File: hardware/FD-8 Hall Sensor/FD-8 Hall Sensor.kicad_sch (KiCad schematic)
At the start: 18 parts, among them J1 Panel connections, J2 ICSP Programming, J3 Hall sensor input, J4 Extra GPIO, U1 LM2940T-5.0_NOPB, U2 ATtiny13A-P, U3 MCP42100

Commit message: update PCB placement
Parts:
- C1, C10, C2, C3, C4, C5, C7, C8, C9: footprint Capacitor_THT:C_Disc_D4.7mm_W2.5mm_P5.00mm -> Capacitor_THT:C_Disc_D4.3mm_W1.9mm_P5.00mm
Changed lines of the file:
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@@
 			)
 		)
-		(property "Footprint" "Capacitor_THT:C_Disc_D4.7mm_W2.5mm_P5.00mm"
+		(property "Footprint" "Capacitor_THT:C_Disc_D4.3mm_W1.9mm_P5.00mm"
 			(at 115.57 48.26 0)
 			(effects
@@
 			)
 		)
-		(property "Footprint" "Capacitor_THT:C_Disc_D4.7mm_W2.5mm_P5.00mm"
+		(property "Footprint" "Capacitor_THT:C_Disc_D4.3mm_W1.9mm_P5.00mm"
 			(at 119.38 48.26 0)
 			(effects
@@
 			)
 		)
-		(property "Footprint" "Capacitor_THT:C_Disc_D4.7mm_W2.5mm_P5.00mm"
+		(property "Footprint" "Capacitor_THT:C_Disc_D4.3mm_W1.9mm_P5.00mm"
 			(at 190.5 48.26 0)
 			(effects
@@
 			)
 		)
-		(property "Footprint" "Capacitor_THT:C_Disc_D4.7mm_W2.5mm_P5.00mm"
+		(property "Footprint" "Capacitor_THT:C_Disc_D4.3mm_W1.9mm_P5.00mm"
 			(at 182.88 48.26 0)
 			(effects
@@
 			)
 		)
-		(property "Footprint" "Capacitor_THT:C_Disc_D4.7mm_W2.5mm_P5.00mm"
+		(property "Footprint" "Capacitor_THT:C_Disc_D4.3mm_W1.9mm_P5.00mm"
 			(at 130.81 48.26 0)
 			(effects
@@
 			)
 		)
-		(property "Footprint" "Capacitor_THT:C_Disc_D4.7mm_W2.5mm_P5.00mm"
+		(property "Footprint" "Capacitor_THT:C_Disc_D4.3mm_W1.9mm_P5.00mm"
 			(at 198.12 48.26 0)
 			(effects
@@
 			)
 		)
-		(property "Footprint" "Capacitor_THT:C_Disc_D4.7mm_W2.5mm_P5.00mm"
+		(property "Footprint" "Capacitor_THT:C_Disc_D4.3mm_W1.9mm_P5.00mm"
 			(at 127 48.26 0)
 			(effects
@@
 			)
 		)
-		(property "Footprint" "Capacitor_THT:C_Disc_D4.7mm_W2.5mm_P5.00mm"
+		(property "Footprint" "Capacitor_THT:C_Disc_D4.3mm_W1.9mm_P5.00mm"
 			(at 123.19 48.26 0)
 			(effects
@@
 			)
 		)
-		(property "Footprint" "Capacitor_THT:C_Disc_D4.7mm_W2.5mm_P5.00mm"
+		(property "Footprint" "Capacitor_THT:C_Disc_D4.3mm_W1.9mm_P5.00mm"
 			(at 127 99.06 0)
 			(effects

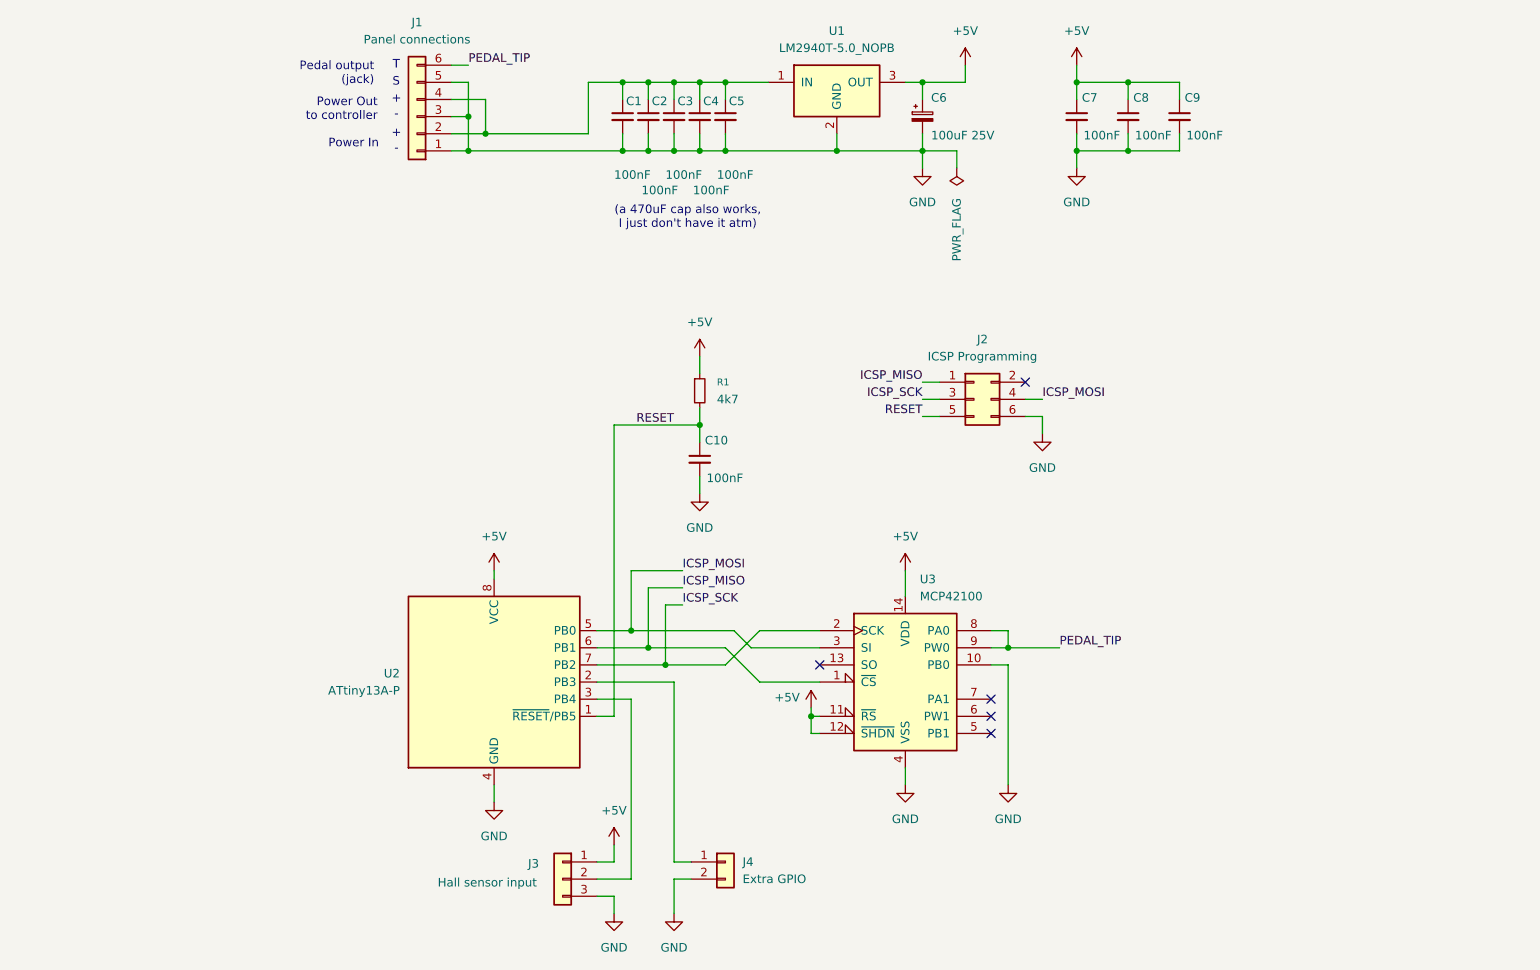
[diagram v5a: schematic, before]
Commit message: use MCP42010 (both pots) instead of MCP42100
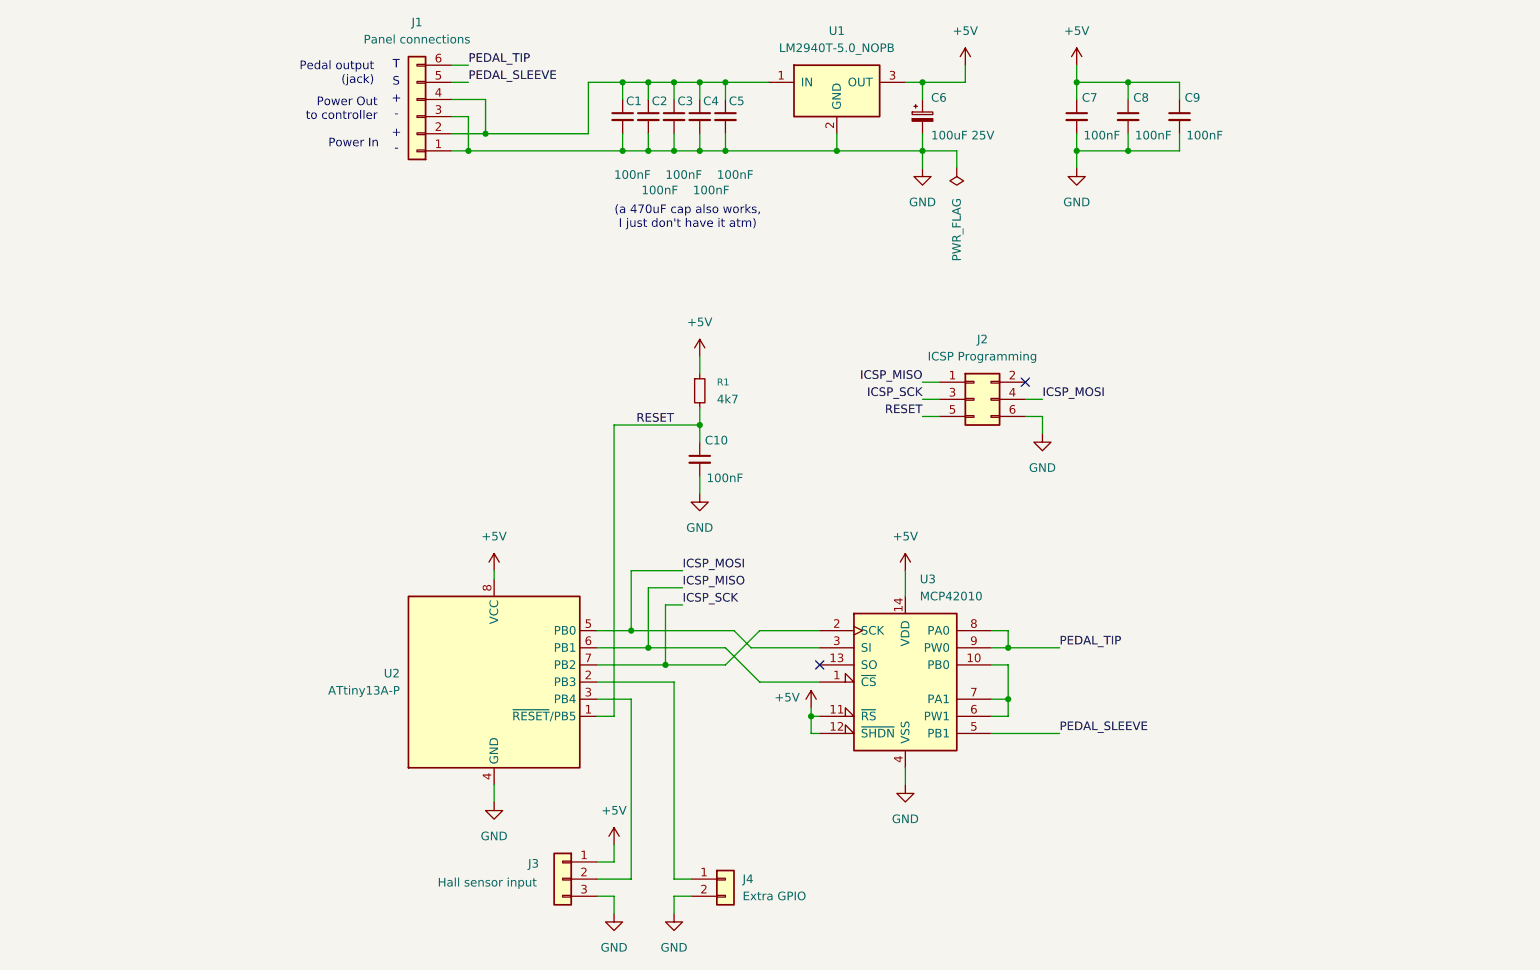
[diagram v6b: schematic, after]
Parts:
- removed U3: MCP42100, Package_DIP:DIP-14_W7.62mm, symbol Potentiometer_Digital:MCP42100
- added U3: MCP42010, Package_DIP:DIP-14_W7.62mm, symbol Potentiometer_Digital:MCP42010
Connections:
- net +5V: now also U3.11 (~{RS}), U3.12 (~{SHDN}), U3.14 (VDD)
- net GND: now also U3.4 (VSS); no longer J1.5 (Pin_5)
- net ICSP_MISO: now also U3.1 (~{CS})
- net ICSP_MOSI: now also U3.3 (SI)
- net ICSP_SCK: now also U3.2 (SCK)
- net PEDAL_TIP: now also U3.8 (PA0), U3.9 (PW0)
- new net: U3.10 (PB0), U3.6 (PW1), U3.7 (PA1)
- new net PEDAL_SLEEVE: J1.5 (Pin_5), U3.5 (PB1)
- no-connect marks 5 -> 2
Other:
- moved on the sheet: J4

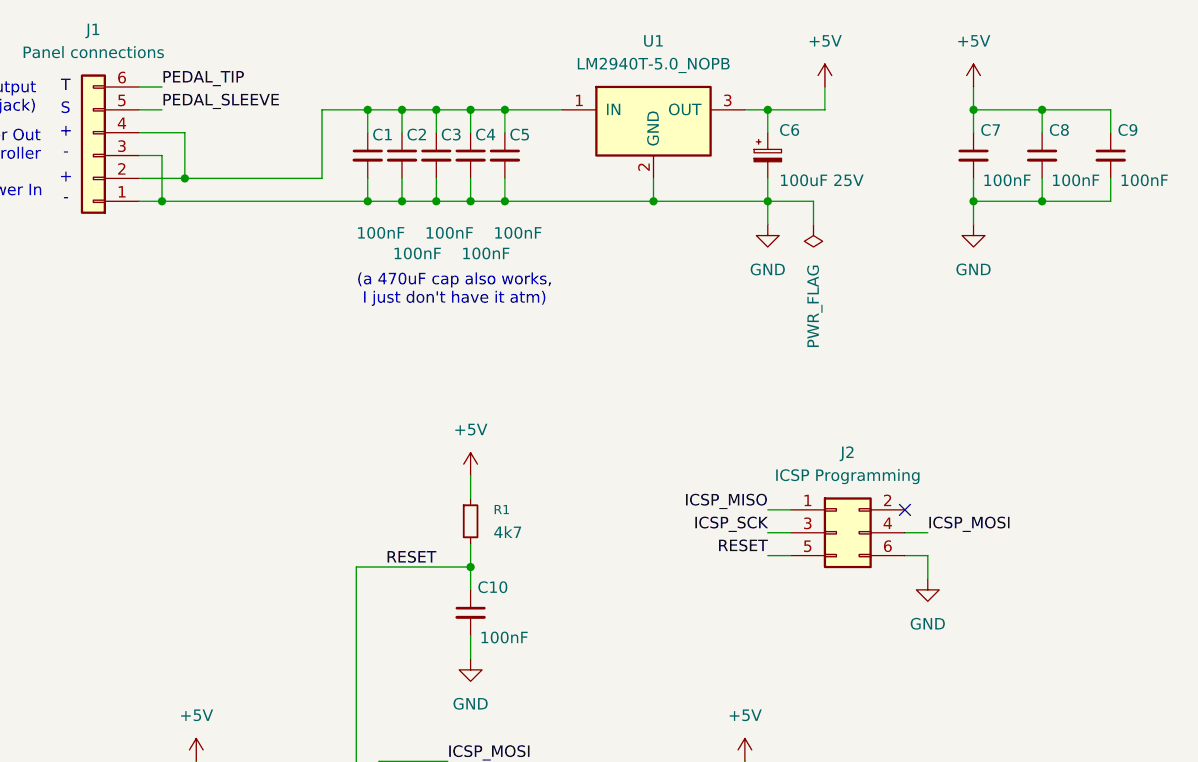
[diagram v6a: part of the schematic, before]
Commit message: fix caps; lock mounting holes
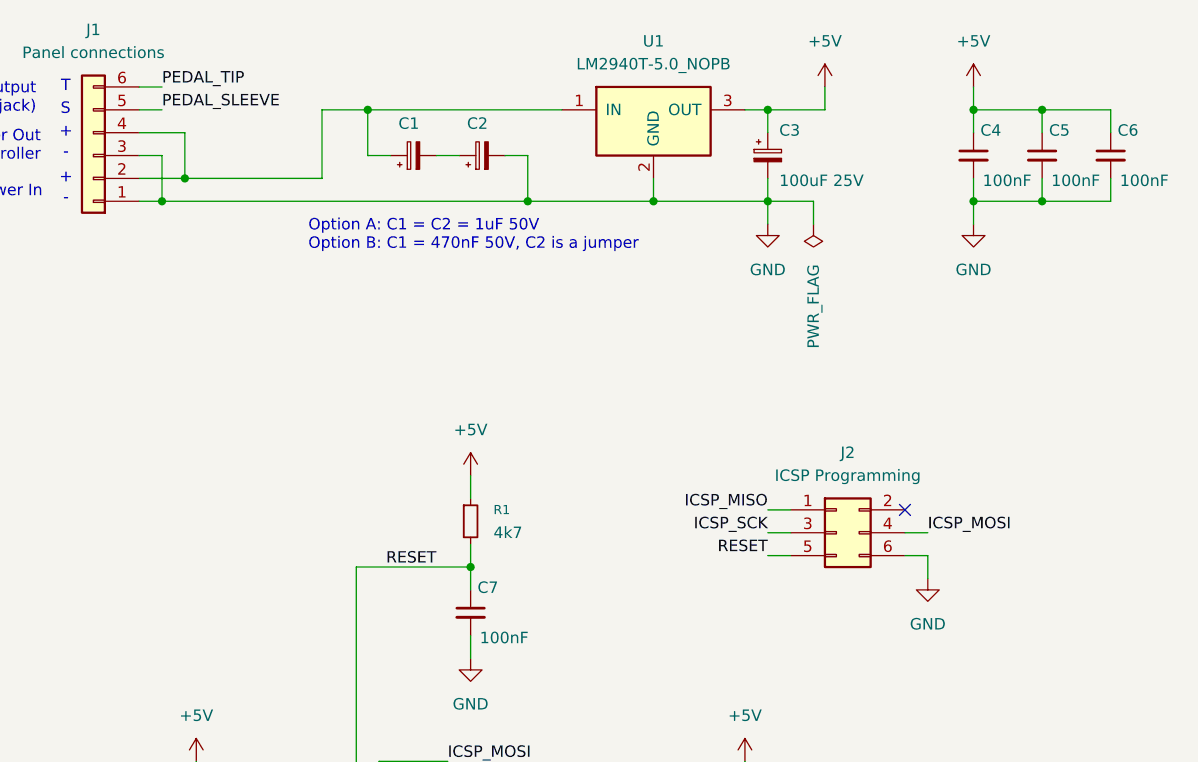
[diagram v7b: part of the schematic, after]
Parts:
- removed C1, C2, C3, C4, C5: 100nF, Capacitor_THT:C_Disc_D4.3mm_W1.9mm_P5.00mm, symbol Device:C_Small
- added C1, C2: ~, Capacitor_THT:CP_Radial_D5.0mm_P2.50mm, symbol Device:C_Polarized_Small
- C3: renamed from C6; footprint Capacitor_THT:CP_Radial_D5.0mm_P2.50mm -> Capacitor_THT:CP_Radial_D6.3mm_P2.50mm
- renumbered C7 to C4, C8 to C5, C9 to C6, C10 to C7
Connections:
- net GND: now also C2.2
- net at J1.2 (Pin_2), J1.4 (Pin_4), U1.1 (IN): now also C1.1
- new net: C1.2, C2.1
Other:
- note added: "Option A: C1 = C2 = 1uF 50V Option B: C1 = 470nF 50V, C2 is a jumper"
- note removed: "(a 470uF cap also works, I just don't have it atm)"
